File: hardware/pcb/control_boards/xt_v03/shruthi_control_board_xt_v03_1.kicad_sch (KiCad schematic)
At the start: 29 parts, among them IC1 24LC512, IC10 ATMEGA644p, J1 CV, J2 POWER, J3 M03PTH, J4 POWER, Q1 20MHz, U1 AVRISP, X1 MIDI, X2 MIDI

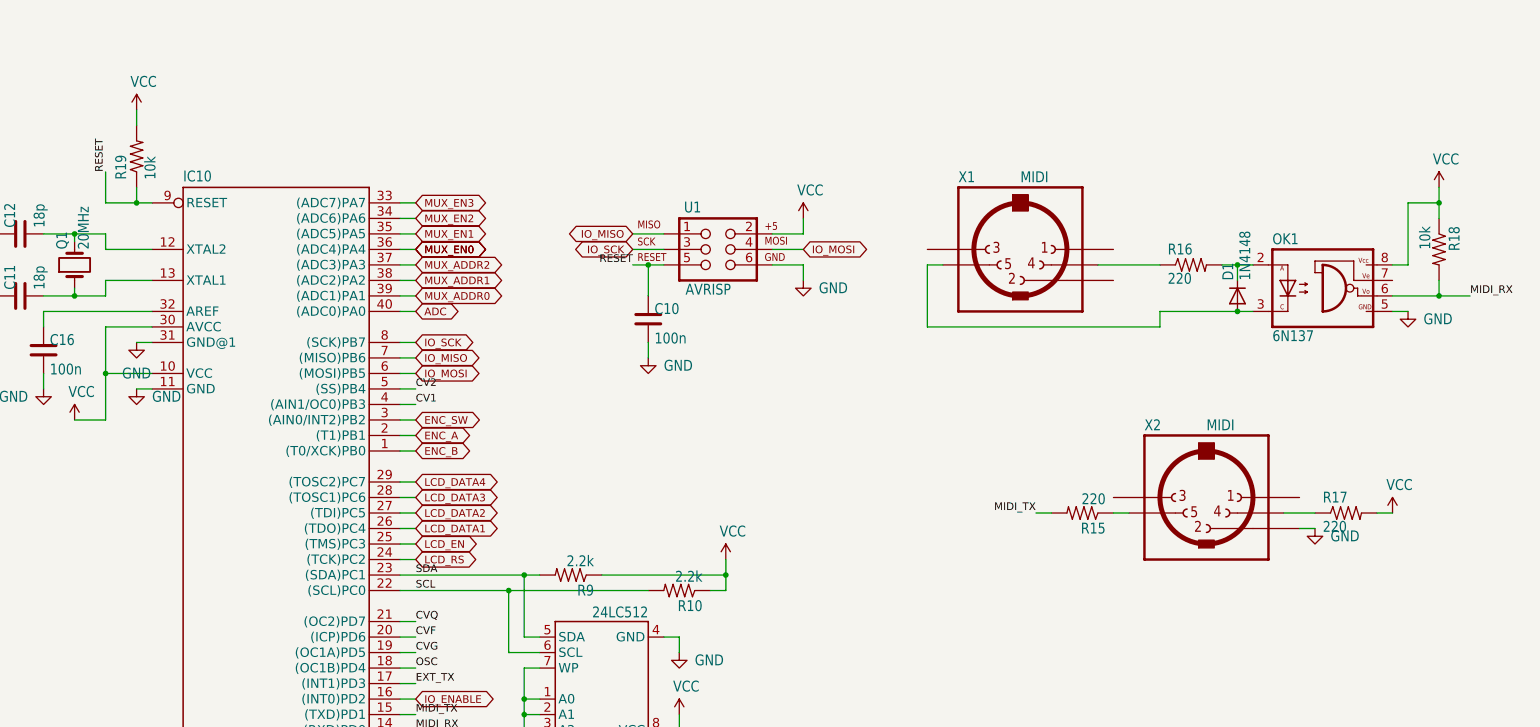
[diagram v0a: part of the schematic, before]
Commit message: update resistors to use kicad symbols
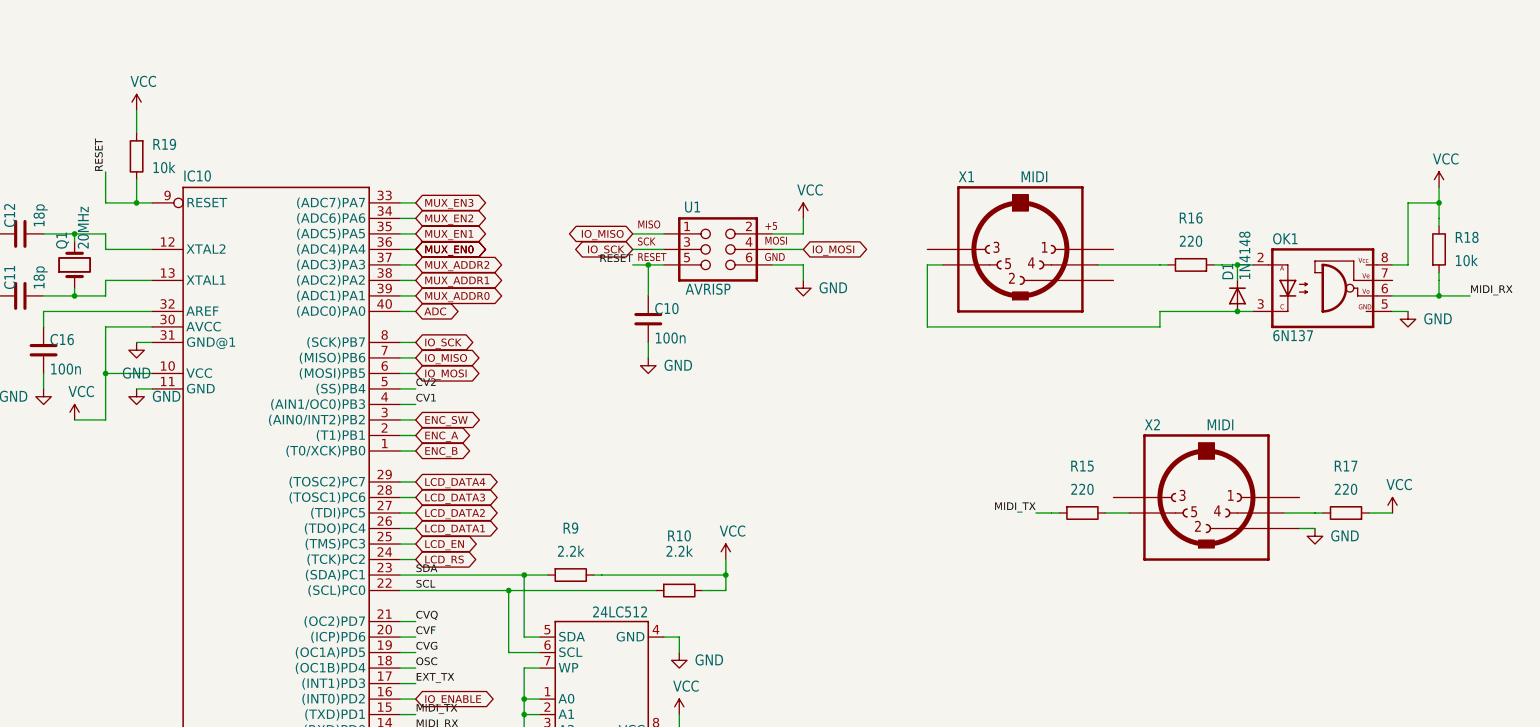
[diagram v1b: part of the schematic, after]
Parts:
- R10, R15, R16, R17, R18, R19, R9: symbol shruthi_control_board_xt_v03-eagle-import:R-US_0204/7 -> Device:R

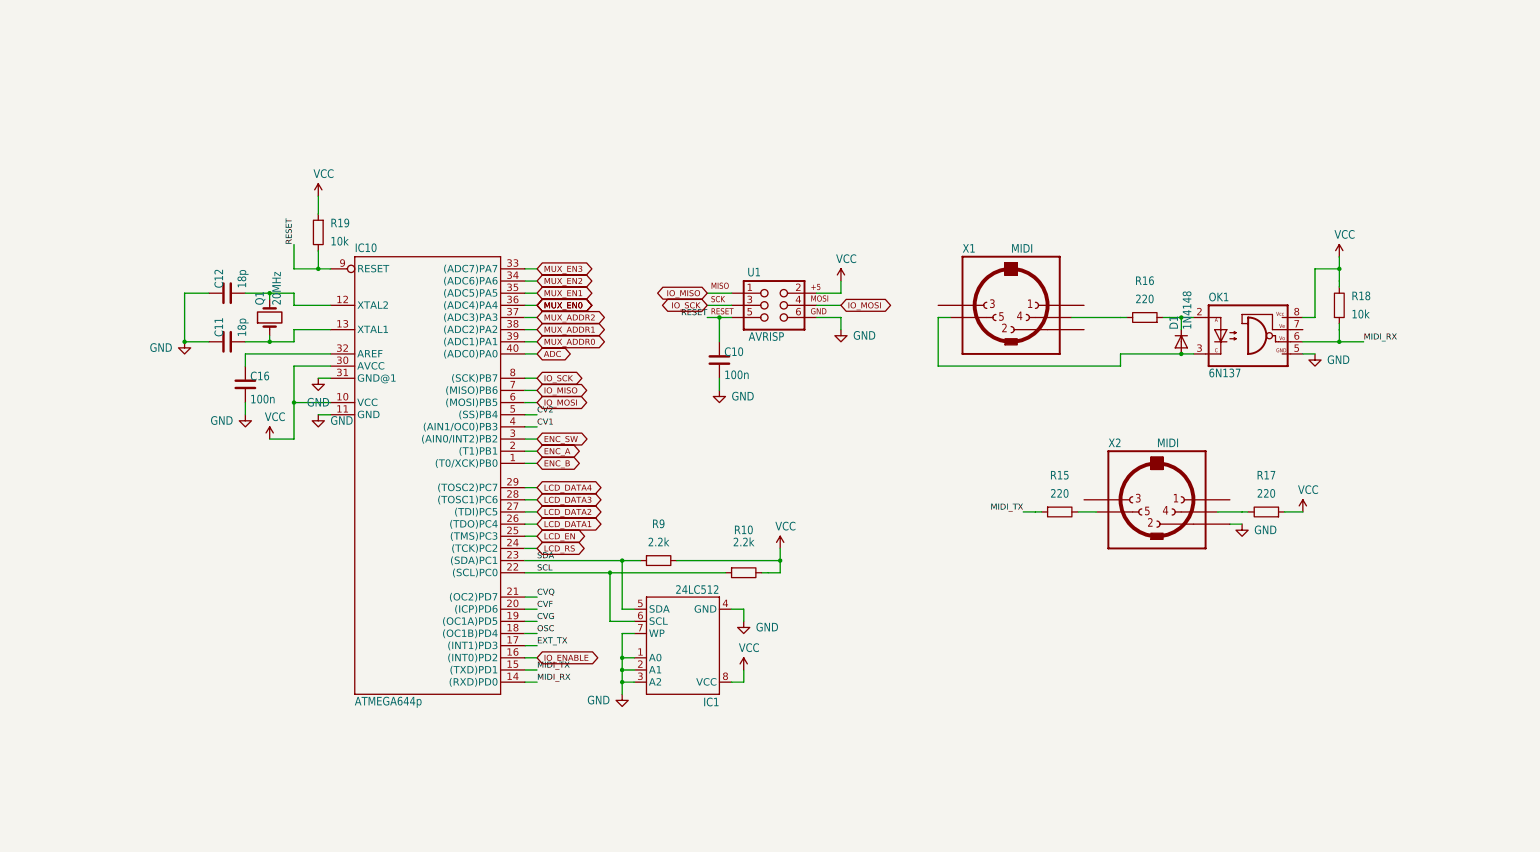
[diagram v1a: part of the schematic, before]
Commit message: update atmega644p to use kicad symbols
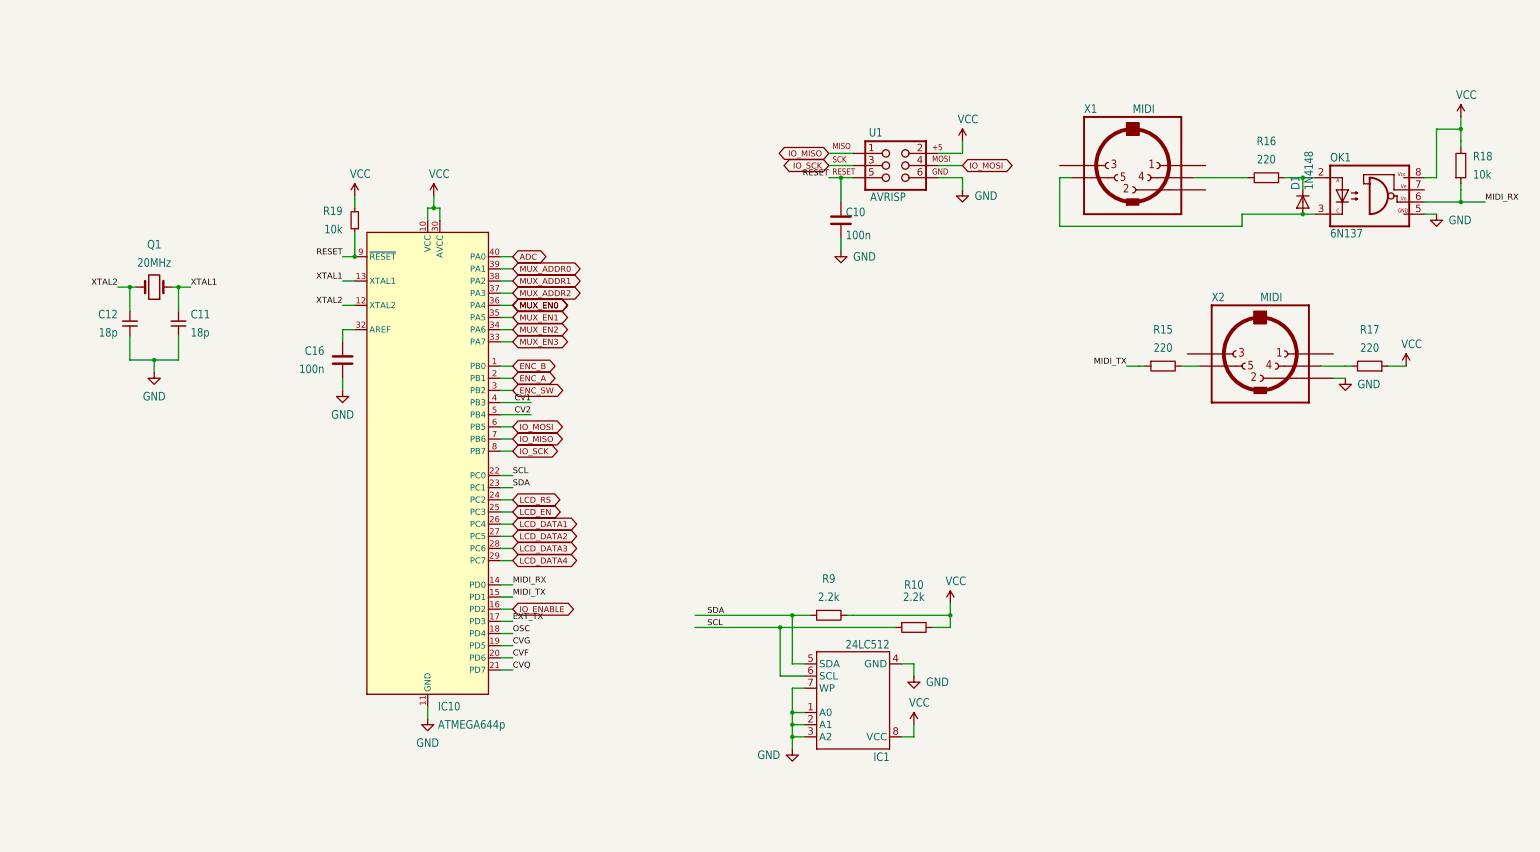
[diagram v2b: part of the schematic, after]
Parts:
- C11, C12: symbol Device:C -> Device:C_Small
- IC10: footprint shruthi_control_board_xt_v03:DIL40 -> Package_DIP:DIP-40_W15.24mm; symbol shruthi_control_board_xt_v03-eagle-import:MEGA16-P -> MCU_Microchip_ATmega:ATmega644P-20P
- R19: symbol Device:R -> Device:R_Small
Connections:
- net XTAL1: now reaches C11.2, IC10.13 (XTAL1), Q1.1
- net XTAL2: now reaches C12.2, IC10.12 (XTAL2), Q1.2
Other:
- moved on the sheet: C10, C11, C12, C16, D1, IC1, OK1, Q1, R10, R15, R16, R17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

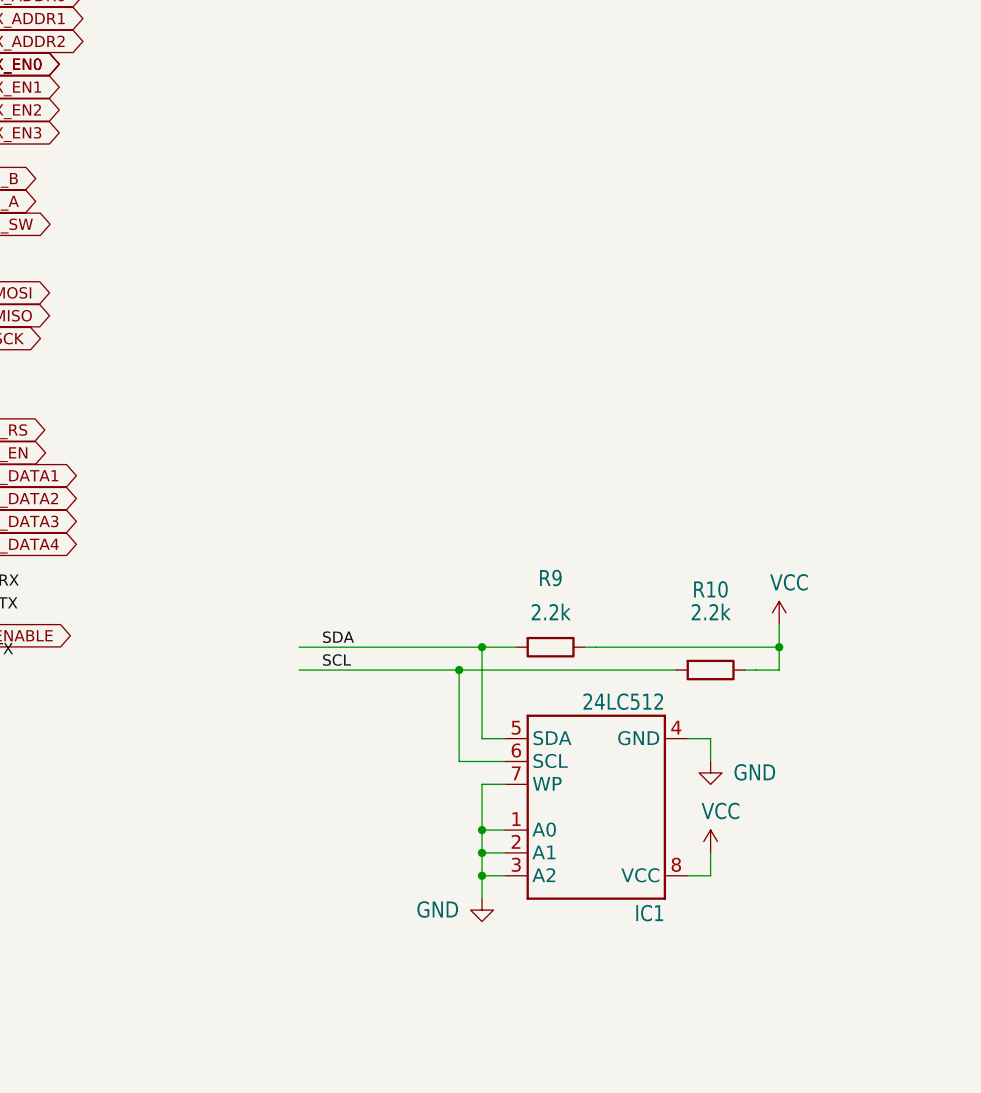
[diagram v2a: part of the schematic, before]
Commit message: update 24LC512 to use kicad symbols
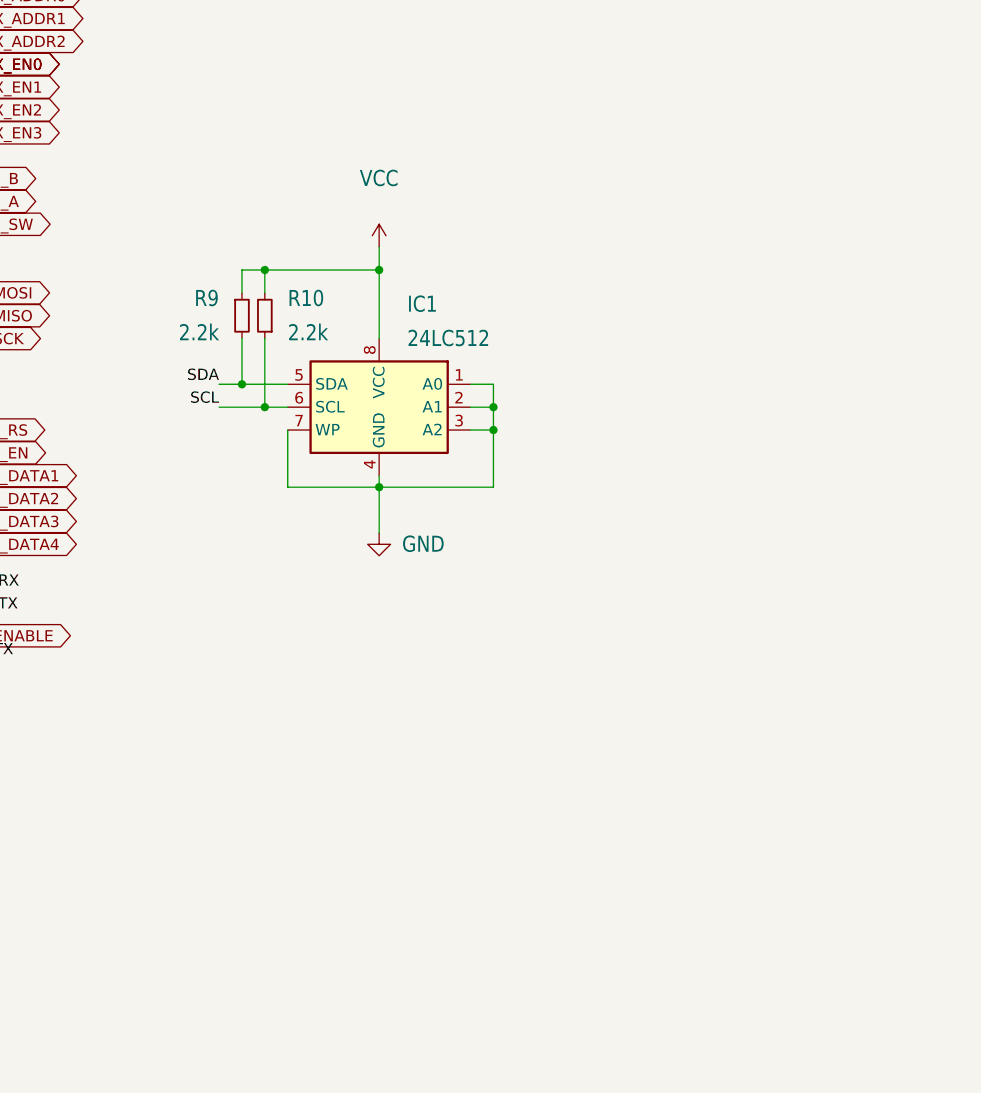
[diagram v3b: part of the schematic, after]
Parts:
- IC1: symbol shruthi_control_board_xt_v03-eagle-import:AT24CP -> Memory_EEPROM:24LC512
- R10, R9: symbol Device:R -> Device:R_Small
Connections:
- net SCL: now also R10.1; no longer R10.2
- net VCC: now also R10.2; no longer R10.1
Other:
- moved on the sheet: R10, R9

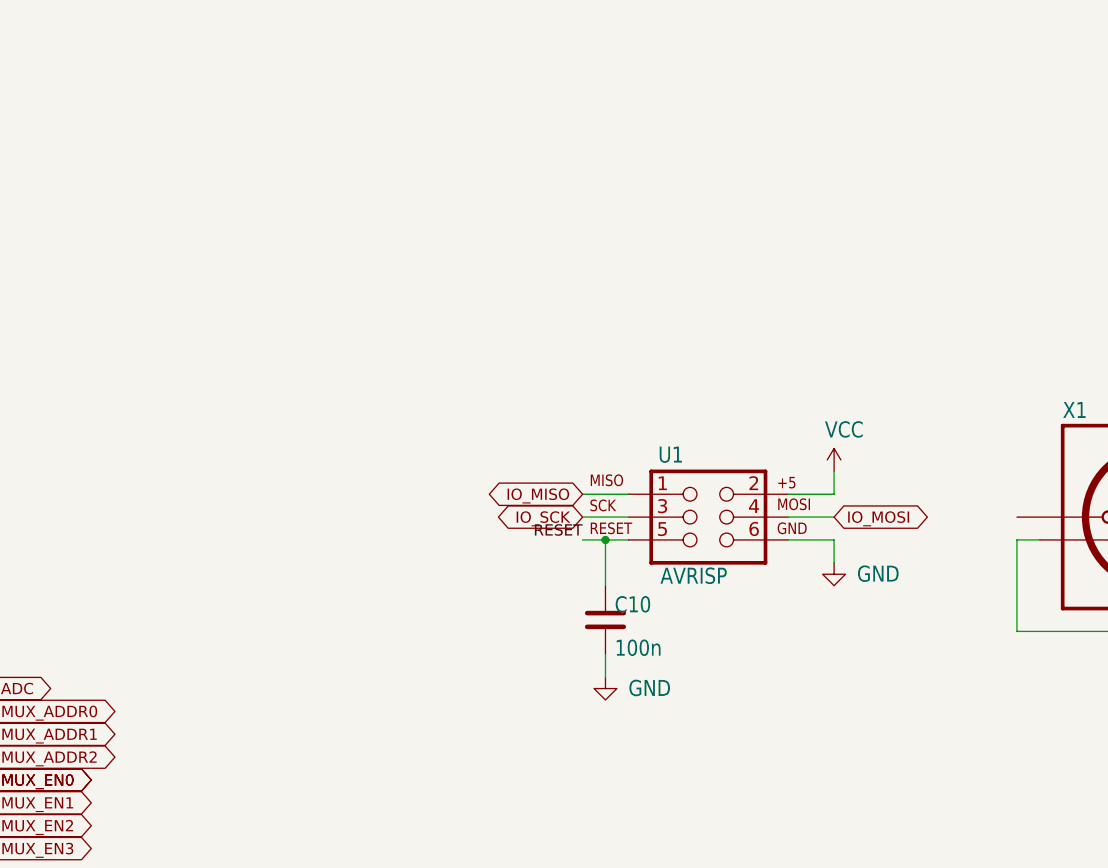
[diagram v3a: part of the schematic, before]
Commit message: update AVR ISP to use kicad symbols
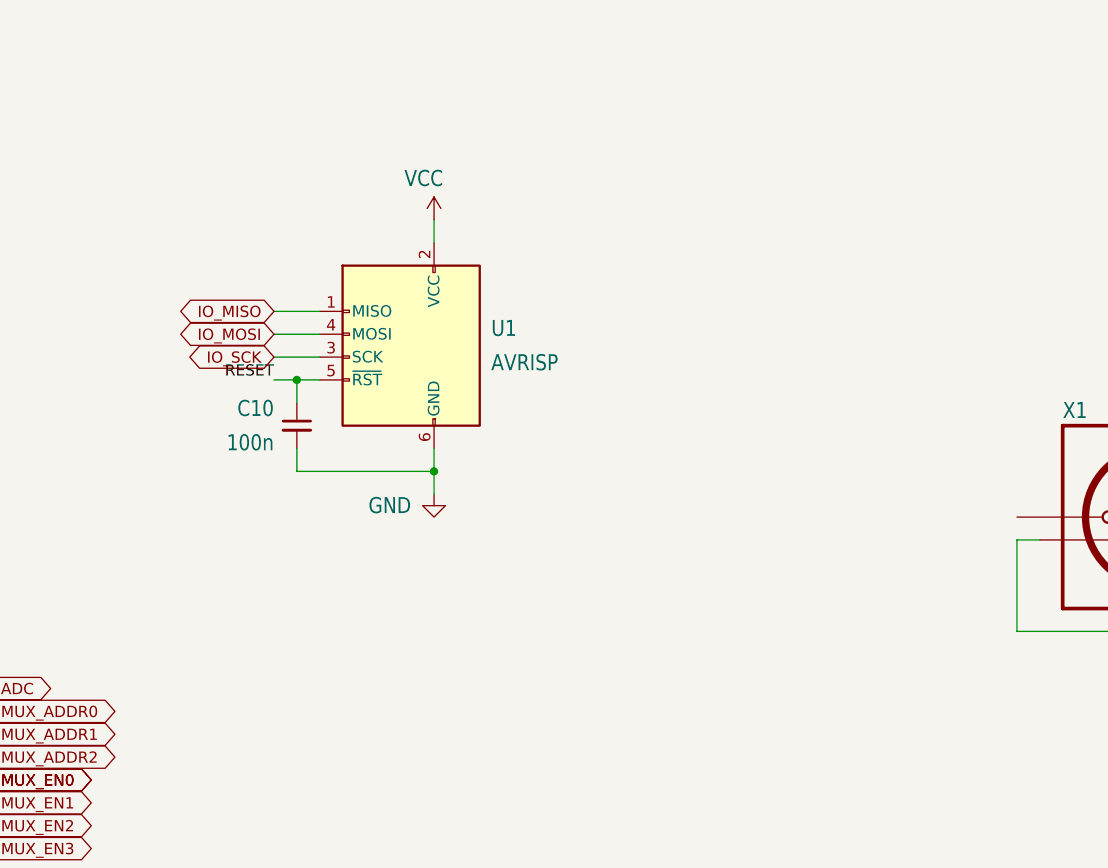
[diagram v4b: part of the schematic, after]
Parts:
- C10: symbol Device:C -> Device:C_Small
- U1: symbol shruthi_control_board_xt_v03-eagle-import:AVR_SPI_PRG_6PTH -> Connector:AVR-ISP-6
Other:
- moved on the sheet: C10
